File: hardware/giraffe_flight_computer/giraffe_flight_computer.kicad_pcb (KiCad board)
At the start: 2 copper layers, 65.4 x 61.6 mm, 139 parts, among them J1 PI_HEADER_HAT, J201 PI_HEADER_SHOE, J202 BAT, J3 SHOE ADC, Q1 DMG2305UX, Q2 DMMT5401, U1 TPS61033, U2 INA180A1, U201 ?, U202 TPS61033, U203 INA180A1, U204 ISO6720B, U205 ISO6720B, U206 PCM2902C, U3 MAX11615, U4 DS18B20, U5 AD1582B, U6 BMI088, U7 BME280, U8 SAM-M8Q, U9 CAT24C32, Y201 12MHz

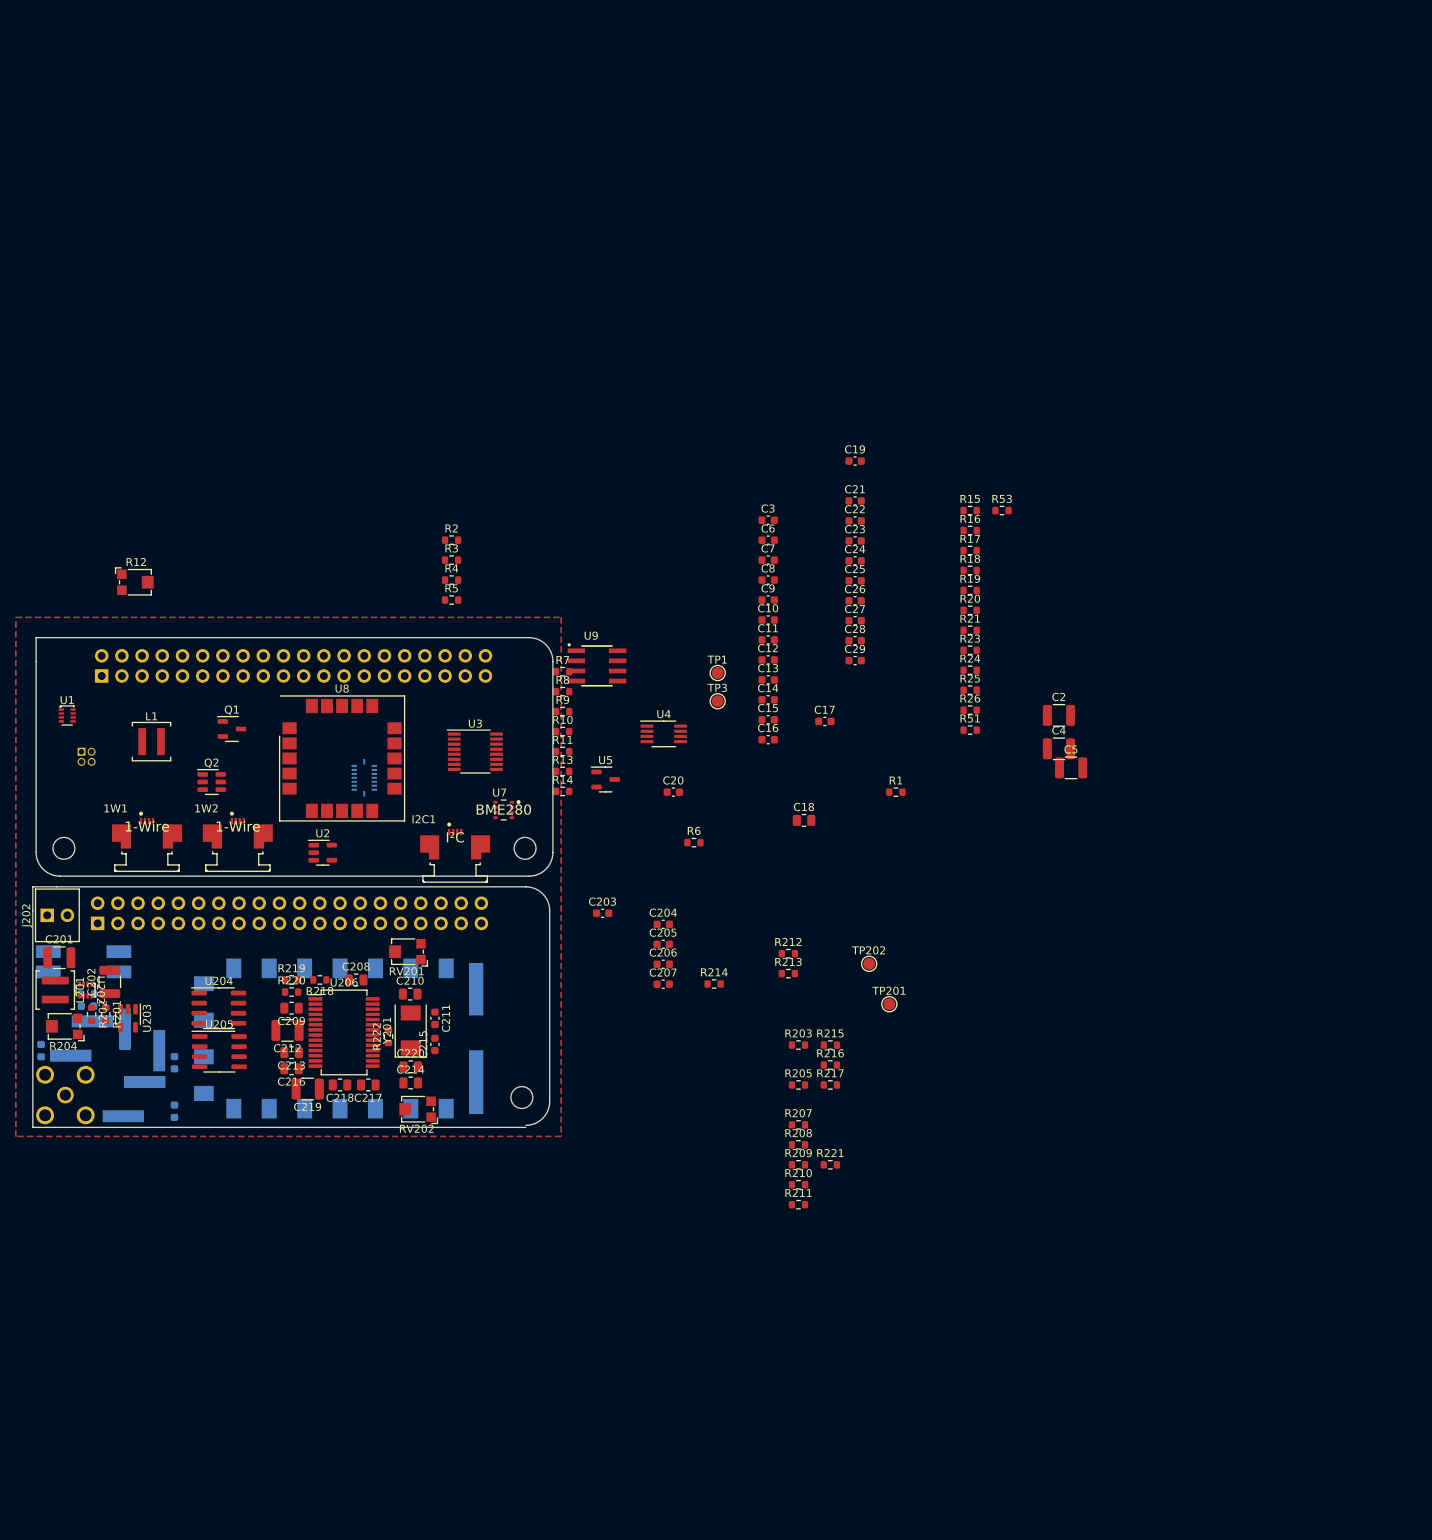
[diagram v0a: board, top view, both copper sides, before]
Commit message: schematic rev A initial design
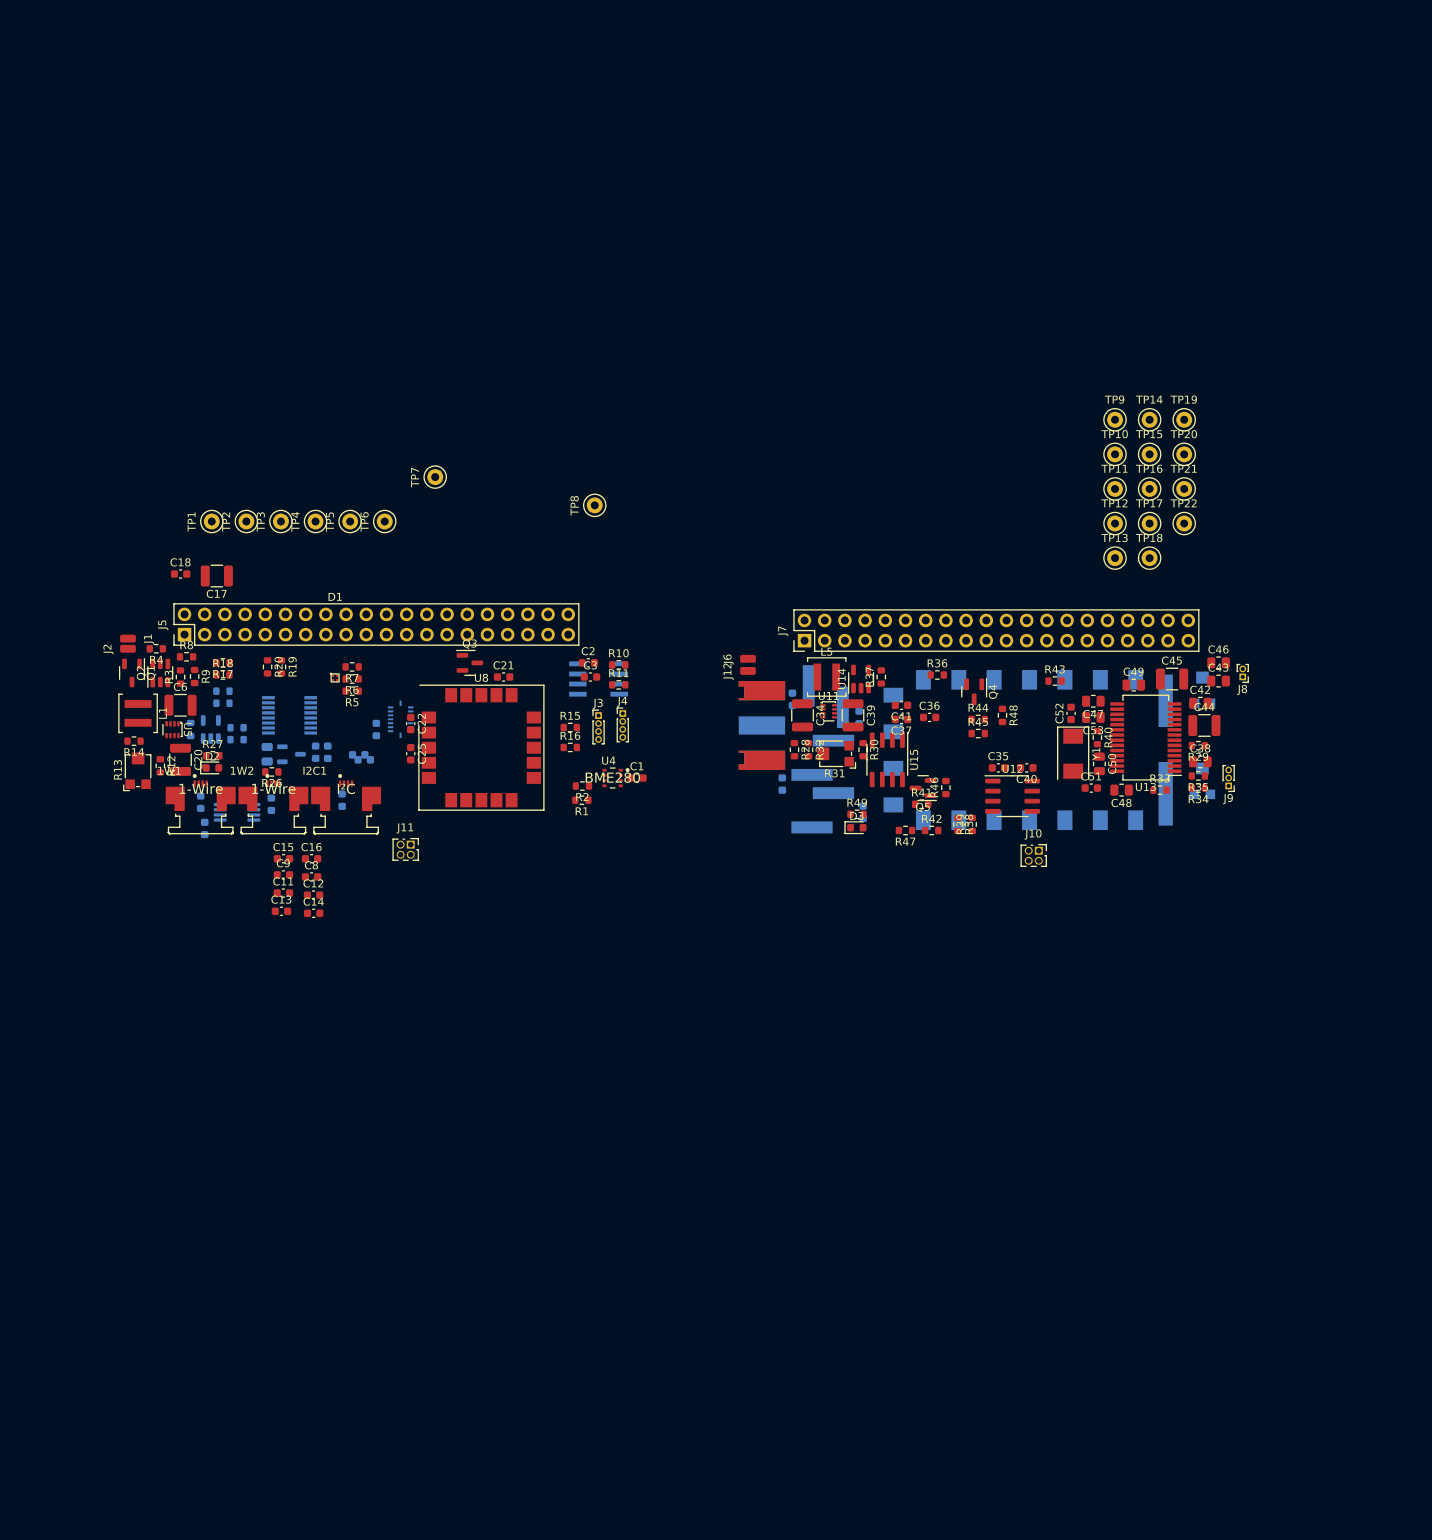
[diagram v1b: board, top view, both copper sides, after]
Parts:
- removed AE201: Antenna, giraffe_flight_computer_footprints:LINX_CONSMA001-G
- removed C10: 100pF, Capacitor_SMD:C_0603_1608Metric
- removed C201, C202, C212, C219: 10μF, Resistor_SMD:R_1210_3225Metric
- removed C203, C206, C207: 0.1µF, Capacitor_SMD:C_0603_1608Metric
- removed C204: 10kpF, Capacitor_SMD:C_0603_1608Metric
- removed C205: 1kpF, Capacitor_SMD:C_0603_1608Metric
- removed C208, C209, C210, C213, C214, C216, C217, C218, C220: 1μF, Resistor_SMD:R_0805_2012Metric
- removed C211, C215: ?pF, Capacitor_SMD:C_0603_1608Metric
- removed C221, C224: 20pF, Capacitor_SMD:C_0603_1608Metric
- removed C222, C223: 36pF, Capacitor_SMD:C_0603_1608Metric
- removed J201: PI_HEADER_SHOE, Connector_PinSocket_2.54mm:PinSocket_2x20_P2.54mm_Vertical
- removed J202: BAT, giraffe_flight_computer_footprints:OSTVN02A150 2x1 Terminal Block
- removed L201: 0.47uH, Inductor_SMD:L_Coilcraft_XAL4020-XXX
- removed L202, L204: 56nH, giraffe_flight_computer_footprints:IND_AIAC-1812-33NK-T
- removed L203: 68nH, giraffe_flight_computer_footprints:IND_AIAC-1812-33NK-T
- removed R201, R202, R203, R205, R206, R207, R208, R209, R210, R211, R212, R215, R216: ?Ω, Resistor_SMD:R_0603_1608Metric
- removed R204: ?Ω, Potentiometer_SMD:Potentiometer_Bourns_TC33X_Vertical
- removed R213, R217: ?kΩ, Resistor_SMD:R_0603_1608Metric
- removed R214: 10kΩ, Resistor_SMD:R_0603_1608Metric
- removed R218: 1.5kΩ, Resistor_SMD:R_0603_1608Metric
- removed R219, R220: 22Ω, Resistor_SMD:R_0603_1608Metric
- removed R221: 2.2Ω, Resistor_SMD:R_0603_1608Metric
- removed R222: 1MΩ, Resistor_SMD:R_0603_1608Metric
- removed R51, R53: 0Ω, Resistor_SMD:R_0603_1608Metric
- removed RV201, RV202: 100kΩ, Potentiometer_SMD:Potentiometer_Bourns_TC33X_Vertical
- removed TP201, TP202: ~, TestPoint:TestPoint_Pad_D1.5mm
- removed TX201: SA868, giraffe_flight_computer_footprints:DORJI_DRA818V
- removed U201: ?, Package_DIP:DIP-4_W8.89mm_SMDSocket_LongPads
- removed U202: TPS61033, Package_TO_SOT_SMD:SOT-583-8
- removed U203: INA180A1, Package_TO_SOT_SMD:SOT-23-5
- removed U204, U205: ISO6720B, Package_SO:SOIC-8_3.9x4.9mm_P1.27mm
- removed U206: PCM2902C, Package_SO:SSOP-28_5.3x10.2mm_P0.65mm
- removed Y201: 12MHz, Crystal:Crystal_SMD_0603-2Pin_6.0x3.5mm
- added AE1: SMA, giraffe_flight_computer_footprints:MolexSmaConnector, B.Cu at (108.2, 34.8)
- added C1: 0.1µF, Capacitor_SMD:C_0603_1608Metric, F.Cu at (97.8, 41.4)
- added C30: 20pF, Capacitor_SMD:C_0603_1608Metric, B.Cu at (126.2, 45.7)
- added C31: 36pF, Capacitor_SMD:C_0603_1608Metric, B.Cu at (116.1, 42.2)
- added C32: 36pF, Capacitor_SMD:C_0603_1608Metric, B.Cu at (125.7, 33.8)
- added C33: 20pF, Capacitor_SMD:C_0603_1608Metric, B.Cu at (117.3, 31.5)
- added C34: 10μF, Resistor_SMD:R_1210_3225Metric, F.Cu at (118.6, 33.5)
- added C35: 0.1µF, Capacitor_SMD:C_0603_1608Metric, F.Cu at (143.3, 40.1)
- added C36: 0.1µF, Capacitor_SMD:C_0603_1608Metric, F.Cu at (134.6, 33.8)
- added C37: 10kpF, Capacitor_SMD:C_0603_1608Metric, F.Cu at (131.1, 34.0)
- added C38: 1μF, Resistor_SMD:R_0805_2012Metric, F.Cu at (168.7, 39.4)
- added C39: 10μF, Resistor_SMD:R_1210_3225Metric, F.Cu at (125.0, 33.5)
- added C40: 0.1µF, Capacitor_SMD:C_0603_1608Metric, F.Cu at (146.8, 40.1)
- added C41: 1kpF, Capacitor_SMD:C_0603_1608Metric, F.Cu at (131.1, 32.3)
- added C42: 1μF, Resistor_SMD:R_0805_2012Metric, F.Cu at (168.7, 32.0)
- added C43: 1μF, Resistor_SMD:R_0805_2012Metric, F.Cu at (170.9, 29.2)
- added C44: 10μF, Resistor_SMD:R_1210_3225Metric, F.Cu at (169.2, 34.8)
- added C45: 10μF, Resistor_SMD:R_1210_3225Metric, F.Cu at (165.1, 29.0)
- added C46: 1μF, Resistor_SMD:R_0805_2012Metric, F.Cu at (170.9, 26.9)
- added C47: 1μF, Resistor_SMD:R_0805_2012Metric, F.Cu at (155.2, 31.8)
- added C48: 1μF, Resistor_SMD:R_0805_2012Metric, F.Cu at (158.8, 42.9)
- added C49: 1μF, Resistor_SMD:R_0805_2012Metric, F.Cu at (160.3, 29.7)
- added C50: 1μF, Resistor_SMD:R_0805_2012Metric, F.Cu at (156.0, 39.6)
- added C51: ?pF, Capacitor_SMD:C_0603_1608Metric, F.Cu at (154.9, 42.7)
- added C52: ?pF, Capacitor_SMD:C_0603_1608Metric, F.Cu at (152.4, 33.3)
- added C53: 1μF, Resistor_SMD:R_0805_2012Metric, F.Cu at (155.2, 33.8)
- added D1: STATUS, giraffe_flight_computer_footprints:B36S3RGB LED, F.Cu at (59.8, 28.8)
- added D2: HAT PWR LED, LED_SMD:LED_0603_1608Metric, F.Cu at (44.4, 40.1)
- added D3: SHOE PWR LED, LED_SMD:LED_0603_1608Metric, F.Cu at (125.5, 47.7)
- added J10: HAT ADC CONNECT, Connector_PinSocket_1.27mm:PinSocket_2x02_P1.27mm_Vertical, F.Cu at (148.3, 50.5)
- added J11: SHOE ADC, Connector_PinSocket_1.27mm:PinSocket_2x02_P1.27mm_Vertical, F.Cu at (69.3, 49.8)
- added J12: BAT-, Connector_Wire:SolderWirePad_1x01_SMD_1x2mm, F.Cu at (111.8, 27.9)
- added J2: BAT-, Connector_Wire:SolderWirePad_1x01_SMD_1x2mm, F.Cu at (33.8, 25.1)
- added J4: EEPROM PROG, Connector_PinHeader_1.00mm:PinHeader_1x04_P1.00mm_Vertical, F.Cu at (96.0, 33.3)
- added J5: PI_HEADER_HAT, giraffe_flight_computer_footprints:pi_zero, F.Cu at (65.0, 22.1)
- added J6: BAT+, Connector_Wire:SolderWirePad_1x01_SMD_1x2mm, F.Cu at (111.8, 26.4)
- added J7: PI_HEADER_SHOE, giraffe_flight_computer_footprints:pi_zero, F.Cu at (143.0, 22.9)
- added J8: Extra Audio, Connector_PinHeader_1.00mm:PinHeader_1x02_P1.00mm_Vertical, F.Cu at (174.0, 28.7)
- added J9: USB, Connector_PinHeader_1.00mm:PinHeader_1x03_P1.00mm_Vertical, F.Cu at (172.2, 42.4)
- added L2: 56nH, giraffe_flight_computer_footprints:IND_AIAC-1812-33NK-T, B.Cu at (121.2, 45.5)
- added L3: 68nH, giraffe_flight_computer_footprints:IND_AIAC-1812-33NK-T, B.Cu at (121.2, 38.9)
- added L4: 56nH, giraffe_flight_computer_footprints:IND_AIAC-1812-33NK-T, B.Cu at (121.5, 31.2)
- added L5: 0.47uH, Inductor_SMD:L_Coilcraft_XAL4020-XXX, F.Cu at (121.7, 28.7)
- added Q3: NPN, Package_TO_SOT_SMD:SOT-23, F.Cu at (76.8, 26.9)
- added Q4: NPN, Package_TO_SOT_SMD:SOT-23, F.Cu at (140.2, 30.6)
- added Q5: NPN, Package_TO_SOT_SMD:SOT-23, F.Cu at (133.8, 42.7)
- added R22: ?Ω, Resistor_SMD:R_0603_1608Metric, B.Cu at (47.5, 35.1)
- added R27: ?Ω, Resistor_SMD:R_0603_1608Metric, F.Cu at (44.5, 38.6)
- added R28: ?Ω, Resistor_SMD:R_0603_1608Metric, F.Cu at (117.6, 37.8)
- added R29: 2.2Ω, Resistor_SMD:R_0603_1608Metric, F.Cu at (168.4, 37.3)
- added R30: ?Ω, Resistor_SMD:R_0603_1608Metric, F.Cu at (126.2, 37.8)
- added R31: ?Ω, Potentiometer_SMD:Potentiometer_Bourns_TC33X_Vertical, F.Cu at (122.7, 38.4)
- added R32: ?Ω, Resistor_SMD:R_0603_1608Metric, F.Cu at (119.4, 37.8)
- added R33: 1.5kΩ, Resistor_SMD:R_0603_1608Metric, F.Cu at (163.6, 42.9)
- added R34: 22Ω, Resistor_SMD:R_0603_1608Metric, F.Cu at (168.4, 42.7)
- added R35: 22Ω, Resistor_SMD:R_0603_1608Metric, F.Cu at (168.4, 41.1)
- added R36: 10kΩ, Resistor_SMD:R_0603_1608Metric, F.Cu at (135.6, 28.4)
- added R37: ?Ω, Resistor_SMD:R_0603_1608Metric, F.Cu at (128.5, 28.7)
- added R38: ?Ω, Resistor_SMD:R_0603_1608Metric, F.Cu at (138.2, 47.2)
- added R39: ?Ω, Resistor_SMD:R_0603_1608Metric, F.Cu at (140.0, 47.2)
- added R40: 1MΩ, Resistor_SMD:R_0603_1608Metric, F.Cu at (155.7, 36.3)
- added R41: ?Ω, Resistor_SMD:R_0603_1608Metric, F.Cu at (133.6, 44.7)
- added R42: ?Ω, Resistor_SMD:R_0603_1608Metric, F.Cu at (134.9, 48.0)
- added R43: ?Ω, Resistor_SMD:R_0603_1608Metric, F.Cu at (150.4, 29.2)
- added R44: ?kΩ, Resistor_SMD:R_0603_1608Metric, F.Cu at (140.7, 34.0)
- added R45: ?Ω, Resistor_SMD:R_0603_1608Metric, F.Cu at (140.7, 35.8)
- added R46: ?Ω, Resistor_SMD:R_0603_1608Metric, F.Cu at (136.7, 42.6)
- added R47: ?kΩ, Resistor_SMD:R_0603_1608Metric, F.Cu at (131.6, 48.0)
- added R48: ?Ω, Resistor_SMD:R_0603_1608Metric, F.Cu at (143.8, 33.5)
- added R49: ?Ω, Resistor_SMD:R_0603_1608Metric, F.Cu at (125.5, 46.0)
- added RV1: 100kΩ, Potentiometer_SMD:Potentiometer_Bourns_TC33X_Vertical, B.Cu at (168.9, 30.2)
- added RV2: 100kΩ, Potentiometer_SMD:Potentiometer_Bourns_TC33X_Vertical, B.Cu at (168.9, 41.7)
- added TP10: ~, TestPoint:TestPoint_Keystone_5000-5004_Miniature, F.Cu at (157.9, 0.70)
- added TP11: ~, TestPoint:TestPoint_Keystone_5000-5004_Miniature, F.Cu at (157.9, 5.05)
- added TP12: ~, TestPoint:TestPoint_Keystone_5000-5004_Miniature, F.Cu at (157.9, 9.40)
- added TP13: ~, TestPoint:TestPoint_Keystone_5000-5004_Miniature, F.Cu at (157.9, 13.7)
- added TP14: ~, TestPoint:TestPoint_Keystone_5000-5004_Miniature, F.Cu at (162.3, -3.65)
- added TP15: ~, TestPoint:TestPoint_Keystone_5000-5004_Miniature, F.Cu at (162.3, 0.70)
- added TP16: ~, TestPoint:TestPoint_Keystone_5000-5004_Miniature, F.Cu at (162.3, 5.05)
- added TP17: ~, TestPoint:TestPoint_Keystone_5000-5004_Miniature, F.Cu at (162.3, 9.40)
- added TP18: ~, TestPoint:TestPoint_Keystone_5000-5004_Miniature, F.Cu at (162.3, 13.7)
- added TP19: ~, TestPoint:TestPoint_Keystone_5000-5004_Miniature, F.Cu at (166.6, -3.65)
- added TP2: ~, TestPoint:TestPoint_Keystone_5000-5004_Miniature, F.Cu at (48.7, 9.14)
- added TP20: ~, TestPoint:TestPoint_Keystone_5000-5004_Miniature, F.Cu at (166.6, 0.70)
- added TP21: ~, TestPoint:TestPoint_Keystone_5000-5004_Miniature, F.Cu at (166.6, 5.05)
- added TP22: ~, TestPoint:TestPoint_Keystone_5000-5004_Miniature, F.Cu at (166.6, 9.40)
- added TP4: ~, TestPoint:TestPoint_Keystone_5000-5004_Miniature, F.Cu at (57.4, 9.14)
- added TP5: ~, TestPoint:TestPoint_Keystone_5000-5004_Miniature, F.Cu at (61.7, 9.14)
- added TP6: ~, TestPoint:TestPoint_Keystone_5000-5004_Miniature, F.Cu at (66.1, 9.14)
- added TP7: ~, TestPoint:TestPoint_Keystone_5000-5004_Miniature, F.Cu at (72.4, 3.56)
- added TP8: ~, TestPoint:TestPoint_Keystone_5000-5004_Miniature, F.Cu at (92.5, 7.11)
- added TP9: ~, TestPoint:TestPoint_Keystone_5000-5004_Miniature, F.Cu at (157.9, -3.65)
- added TX1: SA868, giraffe_flight_computer_footprints:DORJI_DRA818V, B.Cu at (147.2, 37.9)
- added U11: TPS61033, Package_TO_SOT_SMD:SOT-583-8, F.Cu at (121.9, 33.0)
- added U12: ISO6720B, Package_SO:SOIC-8_3.9x4.9mm_P1.27mm, F.Cu at (145.0, 43.7)
- added U13: PCM2902C, Package_SO:SSOP-28_5.3x10.2mm_P0.65mm, F.Cu at (161.8, 36.3)
- added U14: INA180A1, Package_TO_SOT_SMD:SOT-23-5, F.Cu at (126.0, 29.0)
- added U15: ISO6720B, Package_SO:SOIC-8_3.9x4.9mm_P1.27mm, F.Cu at (129.3, 39.1)
- added Y1: 12MHz, Crystal:Crystal_SMD_0603-2Pin_6.0x3.5mm, F.Cu at (152.7, 38.4)
- C11, C12, C13: value 0.1µF -> 100pF
- C17: value 100pF -> 10μF; footprint Capacitor_SMD:C_0603_1608Metric -> Resistor_SMD:R_1210_3225Metric
- C18: value 1μF -> 0.1µF; footprint Resistor_SMD:R_0805_2012Metric -> Capacitor_SMD:C_0603_1608Metric
- C19, C23, C26, C27, C28, C29, R21, R23: moved to B.Cu
- C2: value 10μF -> 0.1µF; footprint Resistor_SMD:R_1210_3225Metric -> Capacitor_SMD:C_0603_1608Metric
- C20, C6: value 0.1µF -> 10μF; footprint Capacitor_SMD:C_0603_1608Metric -> Resistor_SMD:R_1210_3225Metric
- C24: value 0.1µF -> 1μF; footprint Capacitor_SMD:C_0603_1608Metric -> Resistor_SMD:R_0805_2012Metric; moved to B.Cu
- C4, C5: value 10μF -> 0.1µF; footprint Resistor_SMD:R_1210_3225Metric -> Capacitor_SMD:C_0603_1608Metric; moved to B.Cu
- C7: value 100pF -> 0.1µF; moved to B.Cu
- J1: value PI_HEADER_HAT -> BAT+; footprint Connector_PinSocket_2.54mm:PinSocket_2x20_P2.54mm_Vertical -> Connector_Wire:SolderWirePad_1x01_SMD_1x2mm; moved to F.Cu
- J3: value SHOE ADC -> PCM Interface; footprint Connector_PinSocket_1.27mm:PinSocket_2x02_P1.27mm_Vertical -> Connector_PinHeader_1.00mm:PinHeader_1x04_P1.00mm_Vertical; moved to F.Cu
- R1, R2: value ?Ω -> 0Ω
- R10: value 21.5KΩ -> 3.9kΩ
- R11: value ?Ω -> 3.9kΩ
- R12: value 1kΩ -> 21.5KΩ; footprint Potentiometer_SMD:Potentiometer_Bourns_TC33X_Vertical -> Resistor_SMD:R_0603_1608Metric
- R13: value ?Ω -> 1kΩ; footprint Resistor_SMD:R_0603_1608Metric -> Potentiometer_SMD:Potentiometer_Bourns_TC33X_Vertical
- R14: value ?Ω -> 3kΩ
- R16: value 3kΩ -> ?Ω
- R19, R20: value ?Ω -> *
- R24, R25: value 3.9kΩ -> ?Ω; moved to B.Cu
- R26: value ?Ω -> 4.7kΩ
- R6, R7: value * -> ?Ω
- R8: value 4.7kΩ -> ?Ω
- TP1, TP3: footprint TestPoint:TestPoint_Pad_D1.5mm -> TestPoint:TestPoint_Keystone_5000-5004_Miniature
- U1: value TPS61033 -> DS18B20; footprint Package_TO_SOT_SMD:SOT-583-8 -> Package_SO:MSOP-8_3x3mm_P0.65mm; moved to B.Cu
- U2: value INA180A1 -> CAT24C32; footprint Package_TO_SOT_SMD:SOT-23-5 -> giraffe_flight_computer_footprints:CAT24C32WI_GT3; moved to B.Cu
- U3: value MAX11615 -> BMI088; footprint Package_SO:QSOP-16_3.9x4.9mm_P0.635mm -> giraffe_flight_computer_footprints:BMI088; moved to B.Cu
- U4: value DS18B20 -> BME280; footprint Package_SO:MSOP-8_3x3mm_P0.65mm -> giraffe_flight_computer_footprints:BME280
- U5: value AD1582B -> TPS61033; footprint Package_TO_SOT_SMD:SOT-23-3 -> Package_TO_SOT_SMD:SOT-583-8
- U6: value BMI088 -> MAX11615; footprint giraffe_flight_computer_footprints:BMI088 -> Package_SO:QSOP-16_3.9x4.9mm_P0.635mm
- U7: value BME280 -> INA180A1; footprint giraffe_flight_computer_footprints:BME280 -> Package_TO_SOT_SMD:SOT-23-5; moved to B.Cu
- U9: value CAT24C32 -> AD1582B; footprint giraffe_flight_computer_footprints:CAT24C32WI_GT3 -> Package_TO_SOT_SMD:SOT-23-3; moved to B.Cu
- moved C4 107.9 mm to (43.4, 47.8), turned to -90 degrees
- moved R21 98.8 mm to (41.7, 35.3), turned to 90 degrees
- moved R17 95.0 mm to (45.7, 26.9), turned to 180 degrees
- moved R18 94.9 mm to (45.7, 28.4)
- moved R24 94.1 mm to (45.7, 32.0), turned to 180 degrees
- moved R25 94.0 mm to (45.7, 30.5)
- moved R23 92.9 mm to (47.5, 36.6), turned to 180 degrees
- moved R20 88.6 mm to (51.3, 27.4), turned to -90 degrees
- moved C23 88.6 mm to (42.9, 44.5), turned to 90 degrees
- moved R26 88.2 mm to (51.9, 40.6), turned to 180 degrees
- moved C5 87.5 mm to (65.0, 35.3), turned to 90 degrees
- moved R19 87.1 mm to (53.1, 27.4), turned to -90 degrees
- moved C18 84.3 mm to (40.4, 15.7)
- moved C17 78.6 mm to (45.0, 16.0), turned to 180 degrees
- moved C24 77.8 mm to (51.3, 38.4), turned to 90 degrees
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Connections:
- C11 pad 1: H_3V3 -> H_GND
- C11 pad 2: H_GND -> ADC CH2
- C12 pad 1: H_5V_HAT -> H_GND
- C12 pad 2: H_GND -> Net-(J11-Pin_2)
- C13 pad 1: H_5V_HAT -> H_GND
- C13 pad 2: H_GND -> ADC CH1
- C14 pad 2: Net-(J3-Pin_1) -> Net-(J11-Pin_3)
- C15 pad 2: Net-(J3-Pin_2) -> ADC CH0
- C16 pad 2: Net-(J3-Pin_3) -> Net-(J11-Pin_4)
- C17 pad 1: H_GND -> H_5V_HAT
- C17 pad 2: Net-(J3-Pin_4) -> H_GND
- C18 pad 1: 2.5V Reference Voltage -> H_GND
- C18 pad 2: H_GND -> H_5V_HAT
- C19 pad 1: H_GND -> H_3V3
- C19 pad 2: H_3V3 -> H_GND
- C2 pad 1: H_5V_HAT -> H_GND
- C2 pad 2: H_GND -> H_3V3
- C20 pad 1: H_GND -> Net-(U5-VOUT)
- C20 pad 2: H_3V3 -> H_GND
- C21 pad 1: H_GND -> H_3V3
- C21 pad 2: H_3V3 -> H_GND
- C22 pad 1: H_GND -> H_3V3
- C22 pad 2: H_3V3 -> H_GND
- C24 pad 1: H_GND -> Net-(U6-REF)
- C24 pad 2: H_3V3 -> H_GND
- C25 pad 1: H_GND -> H_3V3
- C25 pad 2: H_3V3 -> H_GND
- C26 pad 1: H_3V3 -> H_GND
- C26 pad 2: H_GND -> H_3V3
- C27 pad 1: H_3V3 -> H_GND
- C27 pad 2: H_GND -> H_3V3
- C28 pad 1: H_3V3 -> H_5V_HAT
- C29 pad 1: H_GND -> H_5V_HAT
- C29 pad 2: H_3V3 -> H_GND
- C3 pad 2: H_5V_HAT -> H_3V3
- C4 pad 1: /Battery Polarized -> H_3V3
- C5 pad 1: Net-(U1-VOUT) -> H_GND
- C5 pad 2: H_GND -> H_3V3
- C6 pad 1: H_3V3 -> /Battery Polarized
- C7 pad 2: ADC CH3 -> H_3V3
- C8 pad 2: ADC CH2 -> ADC CH3
- C9 pad 2: ADC CH1 -> Net-(J11-Pin_1)
- J1 pad 1: H_3V3 -> Net-(J1-Pin_1)
- J3 pad 1: Net-(J3-Pin_1) -> /PCM.DOUT
- J3 pad 2: Net-(J3-Pin_2) -> /PCM.DIN
- J3 pad 3: Net-(J3-Pin_3) -> /PCM.FS
- J3 pad 4: Net-(J3-Pin_4) -> /PCM.CLK
- L1 pad 2: Net-(U1-SW) -> Net-(U5-SW)
- Q1 pad 1: Net-(Q1-D) -> Net-(J1-Pin_1)
- Q2 pad 6: Net-(Q1-D) -> Net-(J1-Pin_1)
- R1 pad 2: ADC CH3 -> Net-(U4-SDO)
- R10 pad 1: Net-(U1-VOUT) -> EEPROM.SDA
- R10 pad 2: Net-(R10-Pad2) -> H_3V3
- R11 pad 1: H_5V_HAT -> EEPROM.SCL
- R11 pad 2: ADC CH2 -> H_3V3
- R12 pad 1: Net-(R10-Pad2) -> Net-(U5-VOUT)
- R12 pad 2: Net-(U1-FB) -> Net-(R12-Pad2)
- R13 pad 1: H_5V_HAT -> Net-(R12-Pad2)
- R13 pad 2: Net-(D2-A) -> Net-(U5-FB)
- R14 pad 1: /Battery Polarized -> Net-(U5-FB)
- R14 pad 2: ADC CH0 -> H_GND
- R15 pad 1: ADC CH2 -> Net-(Q3-C)
- R15 pad 2: H_GND -> H_3V3
- R16 pad 1: Net-(U1-FB) -> Net-(Q3-B)
- R16 pad 2: H_GND -> SAM-M8Q.RST
- R17 pad 1: Net-(U2-OUT) -> H_3V3
- R17 pad 2: ADC CH1 -> ADC CH3
- R18 pad 1: ADC CH0 -> ADC CH3
- R19 pad 1: Net-(Q2-B1) -> I2C0.SDA
- R19 pad 2: H_GND -> H_3V3
- R2 pad 1: ADC CH3 -> Net-(U4-SDO)
- R20 pad 1: Net-(Q1-G) -> H_3V3
- R20 pad 2: H_GND -> I2C0.SCL
- R21 pad 1: ADC CH1 -> Net-(U5-VOUT)
- R21 pad 2: H_GND -> H_5V_HAT
- R23 pad 1: Net-(Q3-C) -> ADC CH1
- R23 pad 2: H_3V3 -> H_GND
- R24 pad 1: EEPROM.SDA -> H_5V_HAT
- R24 pad 2: H_3V3 -> ADC CH2
- R25 pad 1: EEPROM.SCL -> ADC CH2
- R25 pad 2: H_3V3 -> H_GND
- R26 pad 1: Net-(Q3-B) -> H_3V3
- R26 pad 2: SAM-M8Q.RST -> 1-Wire
- R3 pad 1: LED.R -> Net-(Q2-B1)
- R3 pad 2: Net-(D1-RK) (its old number) -> H_GND
- R4 pad 1: LED.G -> Net-(Q1-G)
- R4 pad 2: Net-(D1-GK) -> H_GND
- R5 pad 1: LED.B -> /Status LED Red
- R6 pad 1: I2C0.SDA -> /Status LED Green
- R6 pad 2: H_3V3 -> Net-(D1-GK)
- R7 pad 1: H_3V3 -> /Status LED Blue
- R7 pad 2: I2C0.SCL -> Net-(D1-BK)
- R8 pad 1: H_3V3 -> /Battery Polarized
- R8 pad 2: 1-Wire -> ADC CH0
- R9 pad 1: Net-(U1-VOUT) -> ADC CH0
- R9 pad 2: H_5V_HAT -> H_GND
- TP1 pad 1: Net-(U1-SW) -> Net-(J1-Pin_1)
- TP3 pad 1: Net-(U1-PG) -> Net-(U5-PG)
- U1 pad 1: /Battery Polarized -> unconnected-(U1-NC-Pad1)
- U1 pad 2: /Battery Polarized -> unconnected-(U1-NC-Pad2)
- U1 pad 3: H_GND -> H_3V3
- U1 pad 4: Net-(U1-PG) -> 1-Wire
- U1 pad 5: Net-(U1-FB) -> H_GND
- U1 pad 6: H_GND -> unconnected-(U1-NC-Pad6)
- U1 pad 7: Net-(U1-SW) -> unconnected-(U1-NC-Pad7)
- U1 pad 8: Net-(U1-VOUT) -> unconnected-(U1-NC-Pad8)
- U2 pad 1: Net-(U2-OUT) -> H_GND
- U2 pad 3: Net-(U1-VOUT) -> H_GND
- U2 pad 4: H_5V_HAT -> H_GND
- U2 pad 5: H_5V_HAT -> EEPROM.SDA
- U3 pad 1: 2.5V Reference Voltage -> unconnected-(U3-INT2-Pad1)
- U3 pad 10: Net-(J3-Pin_2) -> SPI0.MISO
- U3 pad 11: Net-(J3-Pin_3) -> H_3V3
- U3 pad 12: Net-(J3-Pin_4) -> BMI088.INT3
- U3 pad 13: I2C0.SCL -> unconnected-(U3-INT4-Pad13)
- U3 pad 14: I2C0.SDA -> SPI0.CE0
- U3 pad 15: H_GND -> SPI0.MISO
- U3 pad 16: H_3V3 -> BMI088.INT1
- U3 pad 2: unconnected-(U3-NC-Pad2) -> H_GND
- U3 pad 3: unconnected-(U3-NC-Pad3) -> H_3V3
- U3 pad 4: unconnected-(U3-NC-Pad4) -> H_GND
- U3 pad 5: ADC CH0 -> SPI0.CE1
- U3 pad 6: ADC CH1 -> H_GND
- U3 pad 7: ADC CH2 -> H_GND
- U3 pad 8: ADC CH3 -> SPI0.SCLK
- U3 pad 9: Net-(J3-Pin_1) -> SPI0.MOSI
- U4 pad 1: unconnected-(U4-NC-Pad1) -> H_GND
- U4 pad 2: unconnected-(U4-NC-Pad2) -> H_3V3
- U4 pad 3: H_3V3 -> I2C0.SDA
- U4 pad 4: 1-Wire -> I2C0.SCL
- U4 pad 5: H_GND -> Net-(U4-SDO)
- U4 pad 6: unconnected-(U4-NC-Pad6) -> H_3V3
- U4 pad 7: unconnected-(U4-NC-Pad7) -> H_GND
- U4 pad 8: unconnected-(U4-NC-Pad8) -> H_3V3
- U5 pad 1: 2.5V Reference Voltage -> /Battery Polarized
- U5 pad 2: H_GND -> /Battery Polarized
- U5 pad 3: H_5V_HAT -> H_GND
- U6 pad 1: unconnected-(U6-INT2-Pad1) -> Net-(U6-REF)
- U6 pad 10: SPI0.MISO -> Net-(J11-Pin_2)
- U6 pad 11: H_3V3 -> Net-(J11-Pin_3)
- U6 pad 12: BMI088.INT3 -> Net-(J11-Pin_4)
- U6 pad 13: unconnected-(U6-INT4-Pad13) -> I2C0.SCL
- U6 pad 14: SPI0.CE0 -> I2C0.SDA
- U6 pad 15: SPI0.MISO -> H_GND
- U6 pad 16: BMI088.INT1 -> H_3V3
- U6 pad 2: H_GND -> unconnected-(U6-NC-Pad2)
- U6 pad 3: H_3V3 -> unconnected-(U6-NC-Pad3)
- U6 pad 4: H_GND -> unconnected-(U6-NC-Pad4)
- U6 pad 5: SPI0.CE1 -> ADC CH0
- U6 pad 6: H_GND -> ADC CH1
- U6 pad 7: H_GND -> ADC CH2
- U6 pad 8: SPI0.SCLK -> ADC CH3
- U6 pad 9: SPI0.MOSI -> Net-(J11-Pin_1)
- U7 pad 1: H_GND -> Net-(U7-OUT)
- U7 pad 2: H_3V3 -> H_GND
- U7 pad 3: I2C0.SDA -> Net-(U5-VOUT)
- U7 pad 4: I2C0.SCL -> H_5V_HAT
- U7 pad 5: Net-(U7-SDO) -> H_5V_HAT
- U9 pad 1: H_GND -> Net-(U6-REF)
- U9 pad 3: H_GND -> H_5V_HAT
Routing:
- removed copper zone on B.Cu, net (none)
- removed copper zone on F.Cu, net (none)
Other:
- board outline removed
- copper layers 2 -> 4
- rule pad_to_mask_clearance: 0 -> 0.0381
